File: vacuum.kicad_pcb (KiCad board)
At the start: 2 copper layers, 67 parts, among them J1 к БП, J10 геркон шибера 1, J11 запасной, J12 запасной, J13 к БП, J2 нагрузка, J3 нагрузка, J4 геркон клапана 0, J5 нагрузка, J6 нагрузка, J7 к БП, J8 геркон клапана 1, J9 геркон шибера 0, Q1 IRF740, Q2 IRF740, Q3 IRF740, Q4 IRF740, SW1 Кнопка, SW2 Кнопка, SW3 Кнопка, SW4 Выключить автоматику, SW5 Кнопка, U1 PC817, U10 PC817, U2 PC817, U3 PC817, U4 PC817, U5 PC817, U6 PC817, U7 PC817, U8 PC817, U9 PC817

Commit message: some bags was removed from scheme, mosfet and optrons was added to PCB, watch new txt doc with some pieces of advice
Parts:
- U1, U2, U3, U4: moved to B.Cu
- moved R7 128.0 mm to (90.2, 99.1), turned to 90 degrees
- moved R2 118.2 mm to (94.0, 91.4), turned to 270 degrees
- moved U3 115.4 mm to (115.6, 119.4), turned to 90 degrees
- moved D2 114.3 mm to (86.4, 100.3), turned to 90 degrees
- moved SW3 113.0 mm to (180.3, 143.5)
- moved SW5 113.0 mm to (180.3, 125.7)
- moved U4 110.0 mm to (125.7, 119.4), turned to 90 degrees
- moved U2 88.7 mm to (106.7, 119.4), turned to 90 degrees
- moved Q2 58.5 mm to (80.0, 95.2)
- moved R11 49.5 mm to (97.8, 61.0)
- moved SW2 27.1 mm to (72.4, 91.4), turned to 0 degrees
- moved D1 25.4 mm to (72.4, 118.1), turned to 0 degrees
- moved R10 23.9 mm to (68.6, 100.3), turned to 0 degrees
- moved R1 19.2 mm to (82.5, 113.0), turned to 90 degrees
- moved R4 18.9 mm to (78.7, 106.7), turned to 180 degrees
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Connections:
- R1 pad 2: +5V -> Net-(R1-Pad2)
- R2 pad 2: +5V -> Net-(R2-Pad2)
- R3 pad 2: +5V -> Net-(R3-Pad2)
- R5 pad 2: +5V -> Net-(R5-Pad2)
- U1 pad 3: +5V -> Net-(R1-Pad2)
- U2 pad 3: +5V -> Net-(R2-Pad2)
- U3 pad 3: +5V -> Net-(R3-Pad2)
- U4 pad 3: +5V -> Net-(R5-Pad2)
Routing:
- net Net-(A1-Pad27): track 97.4 -> 249.1 mm
- net Net-(A1-Pad4): track 0.00 -> 137.5 mm
- net +5V: track 162.1 -> 245.0 mm
- net Net-(D1-Pad1): track 8.67 -> 85.7 mm
- net +24V: track 0.00 -> 72.5 mm
- net Net-(D2-Pad2): track 0.00 -> 72.3 mm
- net Net-(D1-Pad2): track 36.3 -> 96.7 mm
- net Net-(A1-Pad6): track 0.00 -> 57.0 mm
- net Net-(R7-Pad1): track 0.00 -> 33.2 mm
- net Net-(R2-Pad2): track 0.00 -> 26.9 mm
- net Net-(R4-Pad1): track 0.00 -> 24.3 mm
- net Net-(A1-Pad9): track 0.00 -> 15.6 mm
- net Net-(Q2-Pad1): track 0.00 -> 15.5 mm
- net Net-(R1-Pad2): track 0.00 -> 15.3 mm
- net Earth: track 390.2 -> 397.8 mm
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
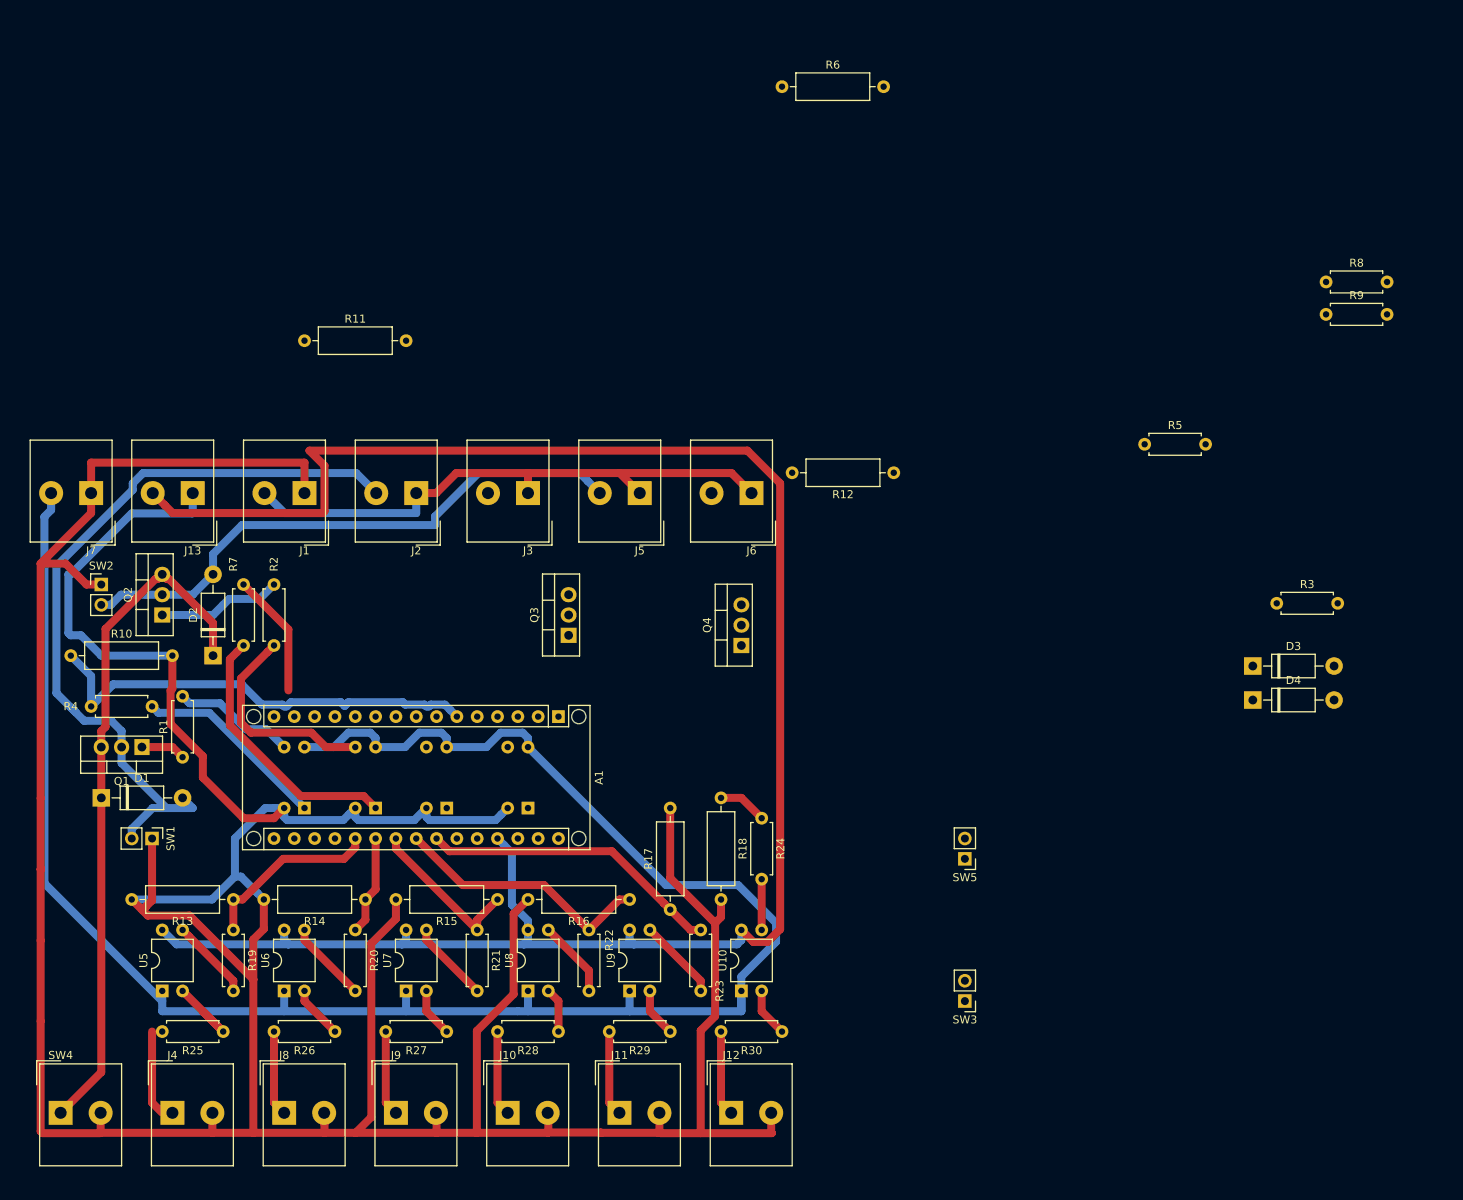
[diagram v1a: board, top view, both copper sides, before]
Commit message: vertical resistors aded
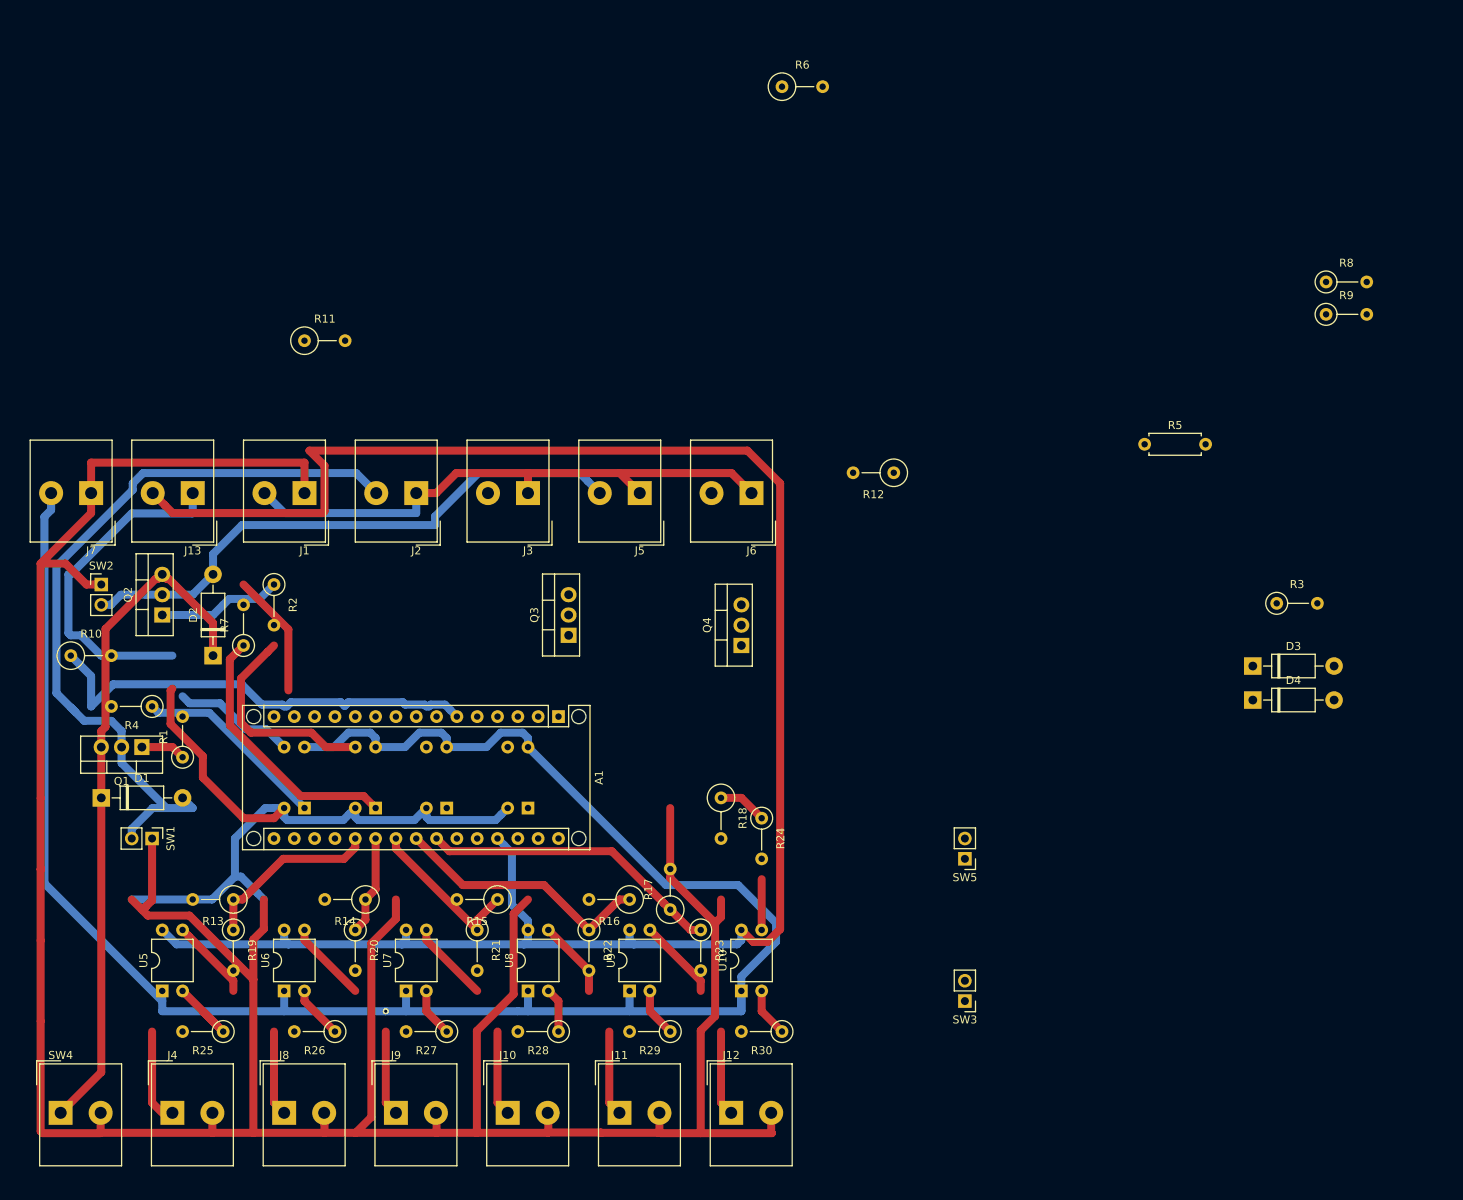
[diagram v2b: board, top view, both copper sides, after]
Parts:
- R1, R19, R2, R20, R21, R22, R23, R24, R25, R26, R27, R28, R29, R3, R30, R4, R7, R8, R9: footprint Resistor_THT:R_Axial_DIN0207_L6.3mm_D2.5mm_P7.62mm_Horizontal -> Resistor_THT:R_Axial_DIN0207_L6.3mm_D2.5mm_P5.08mm_Vertical
- R10, R11, R12, R13, R14, R15, R16, R17, R18, R6: footprint Resistor_THT:R_Axial_DIN0309_L9.0mm_D3.2mm_P12.70mm_Horizontal -> Resistor_THT:R_Axial_DIN0309_L9.0mm_D3.2mm_P5.08mm_Vertical
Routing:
- net Net-(A1-Pad4): track 137.5 -> 133.4 mm
- net +5V: vias 0 -> 1

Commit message: PCB upgrated
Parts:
- R4, R7, R8: moved to B.Cu
- moved R9 159.9 mm to (82.4, 129.0), turned to 180 degrees
- moved D3 150.9 mm to (66.3, 117.8)
- moved R8 145.2 mm to (98.9, 124.7), turned to 90 degrees
- moved R3 144.8 mm to (74.5, 96.1), turned to 270 degrees
- moved R5 140.7 mm to (67.6, 112.7)
- moved R6 131.2 mm to (73.6, 130.0), turned to 180 degrees
- moved D4 129.8 mm to (87.2, 93.3), turned to 270 degrees
- moved SW5 114.7 mm to (69.1, 97.5), turned to 0 degrees
- moved SW3 107.9 mm to (72.7, 135.6), turned to 270 degrees
- moved R10 80.2 mm to (147.9, 112.0)
- moved R11 79.5 mm to (147.2, 123.3)
- moved SW1 72.7 mm to (146.7, 97.4), turned to 0 degrees
- moved D1 70.7 mm to (141.6, 103.8), turned to 90 degrees
- moved Q4 70.7 mm to (81.7, 100.9)
- moved Q3 62.1 mm to (74.0, 122.8), turned to 180 degrees
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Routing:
- net Net-(A1-Pad13): track 0.00 -> 278.6 mm
- net Net-(R5-Pad2): track 0.00 -> 201.2 mm
- net Earth: track 397.8 -> 233.3 mm
- net Net-(A1-Pad4): track 133.4 -> 261.0 mm
- net Net-(R9-Pad1): track 0.00 -> 120.3 mm
- net Net-(A1-Pad27): track 249.1 -> 129.4 mm
- net Net-(R1-Pad2): track 15.3 -> 128.8 mm
- net Net-(D1-Pad2): track 96.7 -> 0.00 mm
- net +24V: track 72.5 -> 0.00 mm
- net Net-(A1-Pad11): track 0.00 -> 63.7 mm
- net Net-(D2-Pad2): track 72.3 -> 22.7 mm
- net Net-(D1-Pad1): track 85.7 -> 50.1 mm
- net Net-(A1-Pad25): track 6.13 -> 37.7 mm
- net Net-(D3-Pad2): track 0.00 -> 28.1 mm
- net Net-(A1-Pad9): track 15.6 -> 43.6 mm
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
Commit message: some pins added, PCB upgrated, it seems to be ready for production
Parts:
- added TP1: TP, Connector_PinHeader_2.54mm:PinHeader_1x02_P2.54mm_Vertical, F.Cu at (97.8, 91.4)
- added TP2: TestPoint, Connector_PinHeader_2.54mm:PinHeader_1x01_P2.54mm_Vertical, F.Cu at (146.1, 90.2)
- R9: moved to B.Cu
- moved R6 76.2 mm to (147.2, 110.5), turned to 0 degrees
- moved R9 52.4 mm to (134.6, 124.5), turned to 90 degrees
- moved SW1 15.9 mm to (130.8, 97.5)
- moved D1 15.5 mm to (153.7, 94.0), turned to 270 degrees
- moved R5 14.9 mm to (69.8, 127.5)
- moved D3 13.8 mm to (78.7, 111.8), turned to 180 degrees
- moved Q1 10.9 mm to (145.9, 101.3), turned to 90 degrees
- moved R1 9.12 mm to (137.5, 96.5)
- moved R13 6.35 mm to (85.1, 135.7)
- moved D2 5.00 mm to (120.7, 93.7)
- moved Q2 4.24 mm to (114.1, 101.3)
- moved R10 3.87 mm to (147.2, 115.8)
- moved R12 3.82 mm to (147.2, 121.3)
- moved R11 3.81 mm to (147.2, 127.1)
- moved Q3 3.60 mm to (71.1, 120.6), turned to 0 degrees
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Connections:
- A1 pad 1: (no net) -> Net-(A1-Pad1)
- A1 pad 10: (no net) -> Net-(A1-Pad10)
- A1 pad 12: (no net) -> Net-(A1-Pad12)
- A1 pad 14: (no net) -> Net-(A1-Pad14)
- A1 pad 15: (no net) -> Net-(A1-Pad15)
- A1 pad 16: (no net) -> Net-(A1-Pad16)
- A1 pad 17: (no net) -> Net-(A1-Pad17)
- A1 pad 18: (no net) -> Net-(A1-Pad18)
- A1 pad 19: (no net) -> Net-(A1-Pad19)
- A1 pad 2: (no net) -> Net-(A1-Pad2)
- A1 pad 26: (no net) -> Net-(A1-Pad26)
- A1 pad 28: (no net) -> Net-(A1-Pad28)
- A1 pad 29: (no net) -> Net-(A1-Pad29)
- A1 pad 3: (no net) -> Net-(A1-Pad3)
- A1 pad 30: (no net) -> Net-(A1-Pad30)
- A1 pad 5: (no net) -> Net-(A1-Pad5)
- A1 pad 7: (no net) -> Net-(A1-Pad7)
- A1 pad 8: (no net) -> Net-(A1-Pad8)
- D4 pad 1: Net-(D3-Pad2) -> Net-(D4-Pad1)
- Q4 pad 3: Net-(D3-Pad2) -> Net-(D4-Pad1)
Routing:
- net Net-(A1-Pad13): track 278.6 -> 66.4 mm
- net Net-(D1-Pad1): track 50.1 -> 188.9 mm
- net Net-(R9-Pad1): track 120.3 -> 5.16 mm
- net Net-(D3-Pad2): track 28.1 -> 132.6 mm
- net Net-(A1-Pad27): track 129.4 -> 225.4 mm
- net Net-(R1-Pad2): track 128.8 -> 38.7 mm
- net Net-(R5-Pad2): track 201.2 -> 127.6 mm, vias 0 -> 1
- net Net-(D4-Pad2): track 21.8 -> 95.2 mm
- net +24V: track 0.00 -> 70.4 mm
- net Net-(D1-Pad2): track 0.00 -> 64.2 mm
- net Net-(A1-Pad4): track 261.0 -> 201.8 mm
- net Earth: track 233.3 -> 274.4 mm
- net Net-(D2-Pad2): track 22.7 -> 55.5 mm
- net Net-(D4-Pad1): track 0.00 -> 16.2 mm
- net +5V: track 239.2 -> 252.3 mm
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
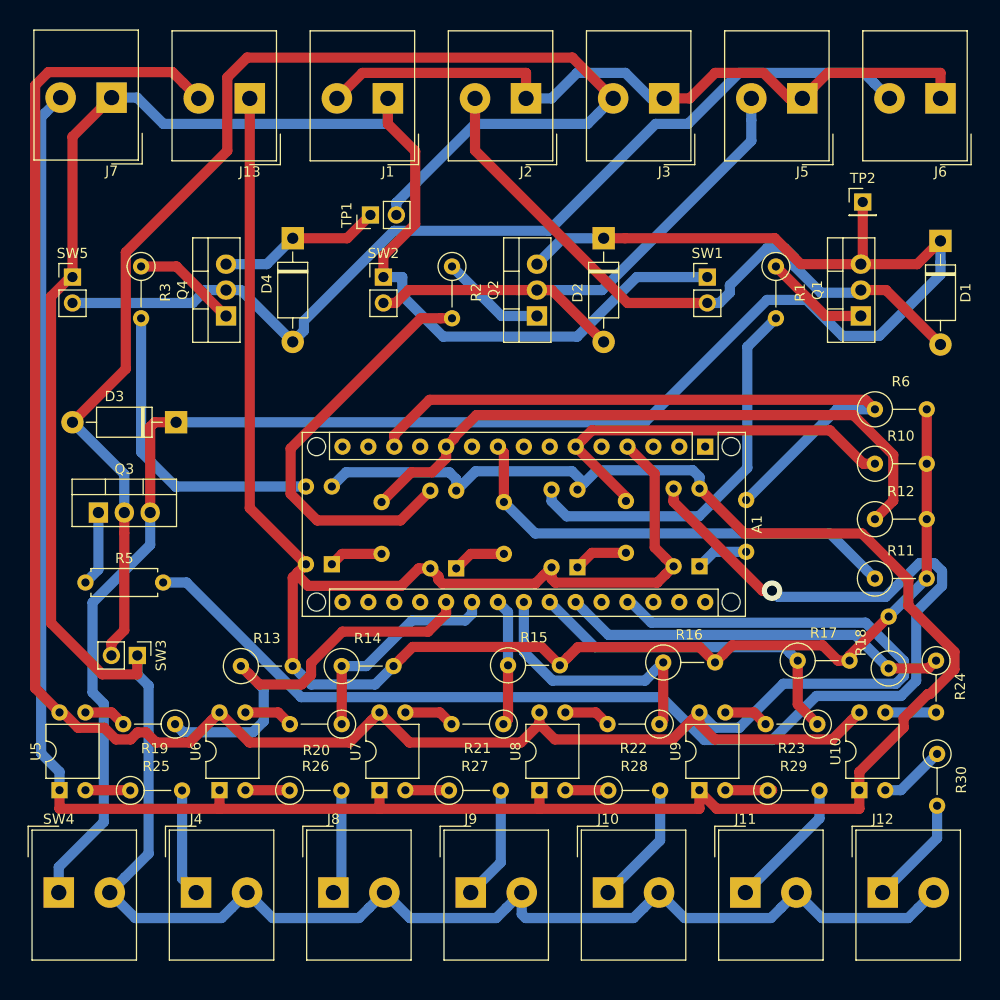
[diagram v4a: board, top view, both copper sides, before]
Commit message: edge added to the PCB
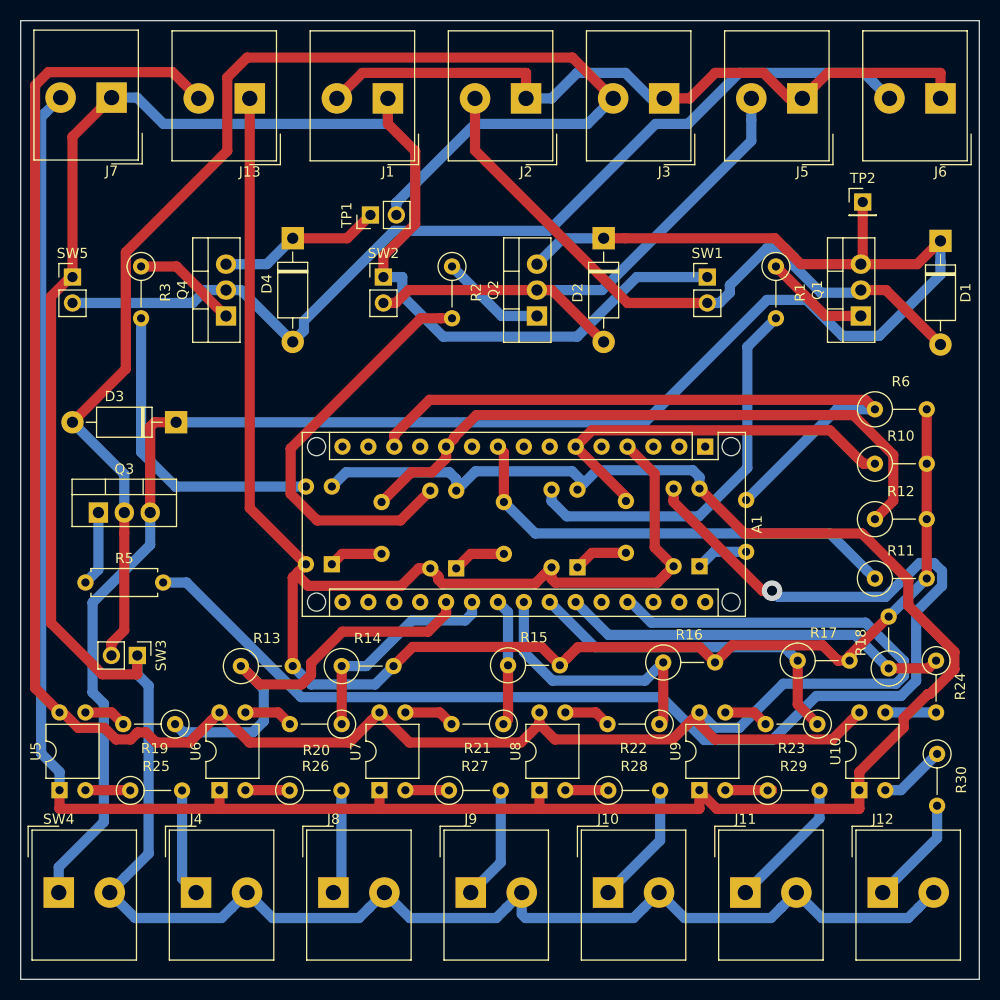
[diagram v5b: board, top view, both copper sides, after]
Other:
- board outline added: 94 x 94 mm
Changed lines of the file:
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@@
   (general
     (thickness 1.6)
-    (drawings 0)
+    (drawings 4)
     (tracks 476)
     (zones 0)
@@
     )
   )
+  (gr_line (start 63.5 166.37) (end 63.5 72.39) (layer Edge.Cuts) (width 0.05))
+  (gr_line (start 157.48 166.37) (end 63.5 166.37) (layer Edge.Cuts) (width 0.05))
+  (gr_line (start 157.48 72.39) (end 157.48 166.37) (layer Edge.Cuts) (width 0.05))
+  (gr_line (start 63.5 72.39) (end 157.48 72.39) (layer Edge.Cuts) (width 0.05))
   (segment (start 143.51 110.49) (end 134.62 119.38) (width 1) (layer B.Cu) (net 1))
   (segment (start 147.2438 110.49) (end 143.51 110.49) (width 1) (layer B.Cu) (net 1))
